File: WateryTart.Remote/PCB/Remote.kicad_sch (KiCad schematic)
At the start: 24 parts, among them J1 Conn_01x04, J2 Conn_01x06, SW1 SW_Push, U1 lolin32_lite_V1.00

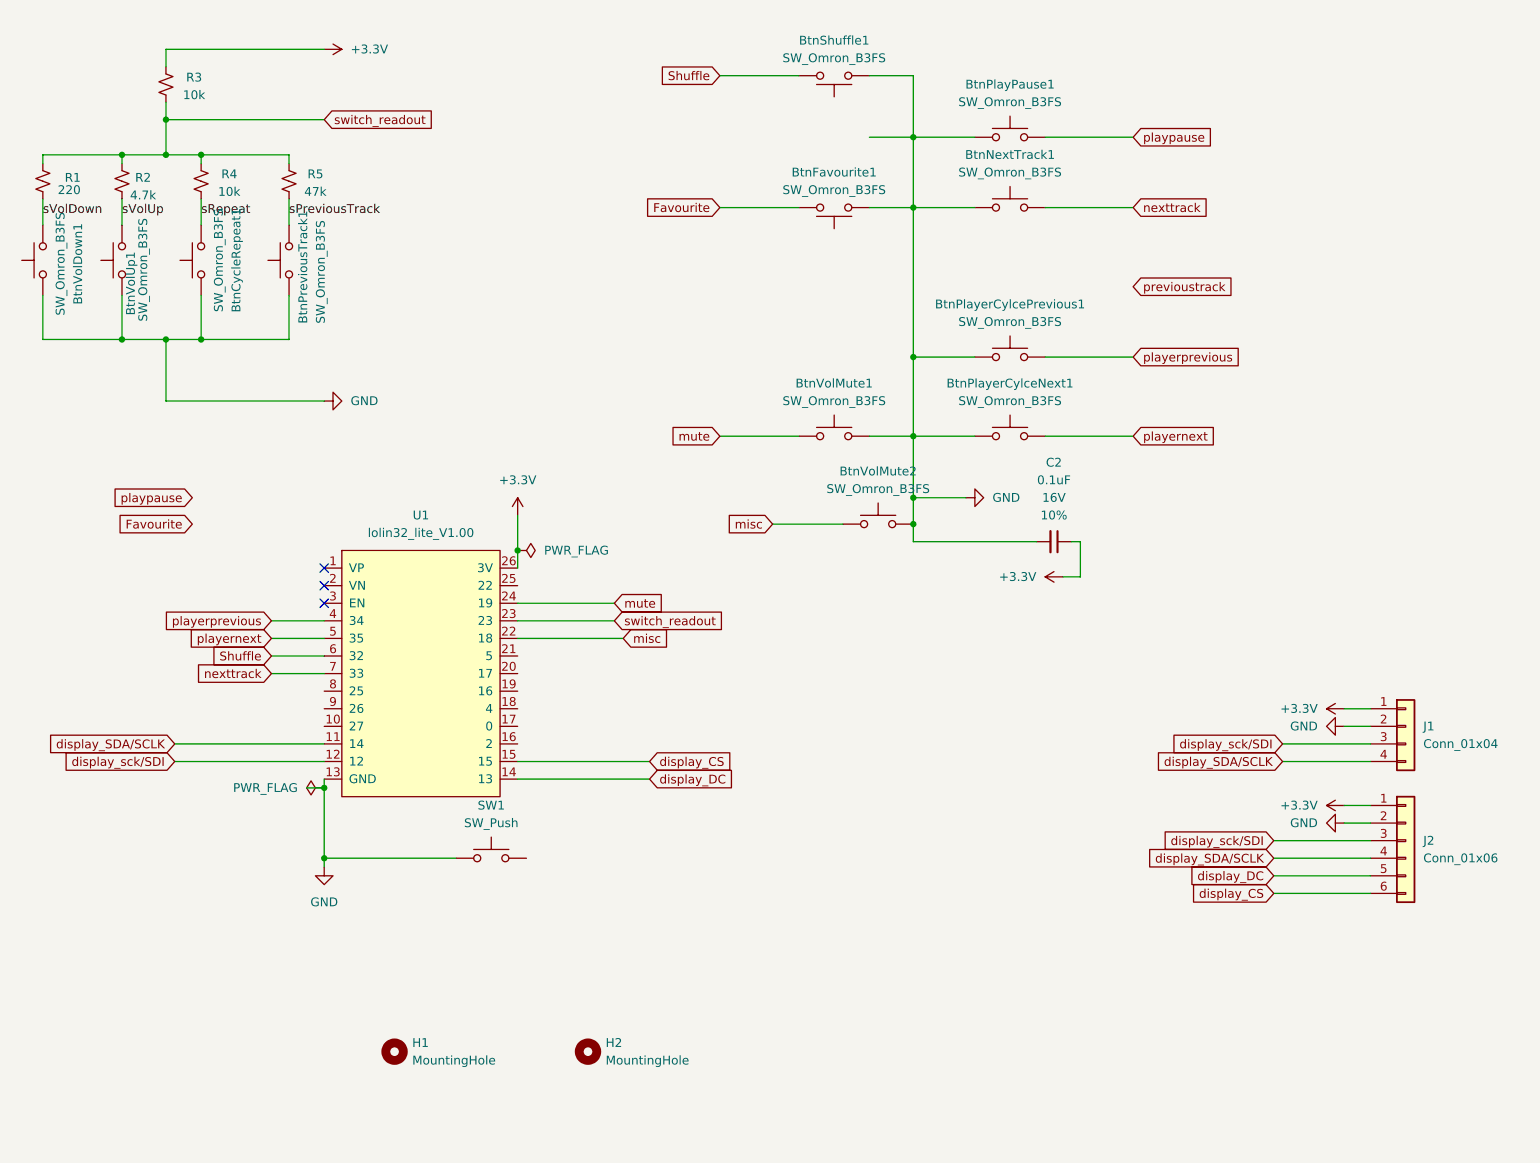
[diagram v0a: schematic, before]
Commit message: Finalised schematic and pcb layout ready for first round of mfg
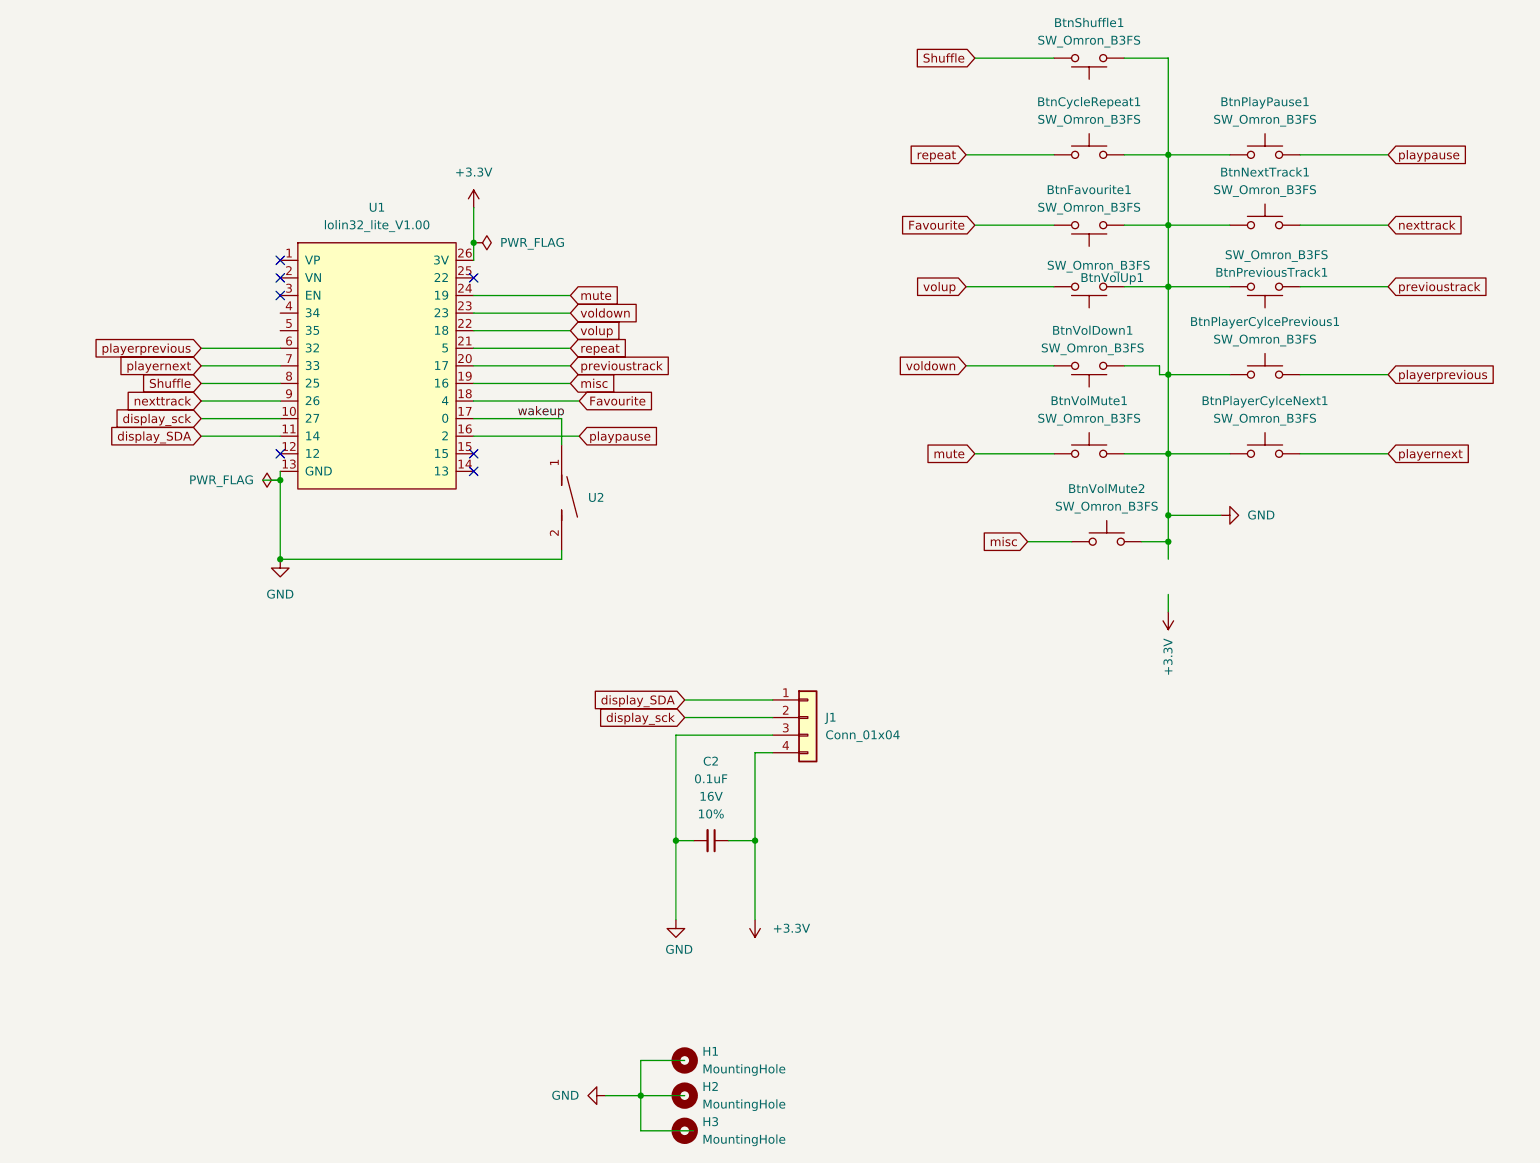
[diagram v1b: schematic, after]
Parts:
- removed J2: Conn_01x06, PCM_SparkFun-Connector:1x06_P2.54mm, symbol PCM_SparkFun-Connector:Conn_01x06_P2.54mm_Socket_Vertical_SMD_Combined
- removed R1: 220, Resistor_THT:R_Axial_DIN0204_L3.6mm_D1.6mm_P5.08mm_Horizontal, symbol PCM_SparkFun-Resistor:3.3k_0402
- removed R2: 4.7k, Resistor_THT:R_Axial_DIN0204_L3.6mm_D1.6mm_P5.08mm_Horizontal, symbol PCM_SparkFun-Resistor:10k_0402
- removed R3, R4: 10k, Resistor_THT:R_Axial_DIN0204_L3.6mm_D1.6mm_P5.08mm_Horizontal, symbol PCM_SparkFun-Resistor:10k_0402
- removed R5: 47k, Resistor_THT:R_Axial_DIN0204_L3.6mm_D1.6mm_P5.08mm_Horizontal, symbol PCM_SparkFun-Resistor:10k_0402
- removed SW1: SW_Push, Resistor_THT:R_Axial_DIN0204_L3.6mm_D1.6mm_P5.08mm_Horizontal, symbol Switch:SW_Push
- added H3: MountingHole, MountingHole:MountingHole_3.2mm_M3_Pad, symbol Mechanical:MountingHole
- added U2: (no value), EasyEDA_Lib:SW-TH_BD3.6-L10.6-LS12.6-D0.4, symbol EasyEDA_Lib:SW-200D 053
- J1: footprint PCM_SparkFun-Connector:1x04_P2.54mm -> Connector_PinSocket_2.54mm:PinSocket_1x04_P2.54mm_Vertical
- U1: footprint PaulsCoolKicadLibrary:WEMOS_LOLIN32_LITE -> Paul:WEMOS_LOLIN32_LITE
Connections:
- net sPreviousTrack is gone; now on net GND: BtnPreviousTrack1.2
- net sRepeat is gone; now on net GND: BtnCycleRepeat1.2
- net switch_readout is gone; now on net voldown: U1.23
- net +3.3V: now also J1.4 (Pin_4); no longer J1.1 (Pin_1)
- net Favourite: now also U1.18 (4)
- net GND: now also J1.3 (Pin_3), U2.2; no longer BtnCycleRepeat1.1, BtnPreviousTrack1.1, J1.2 (Pin_2)
- net Shuffle: now also U1.8 (25); no longer U1.6 (32)
- net misc: now also U1.19 (16); no longer U1.22 (18)
- net nexttrack: now also U1.9 (26); no longer U1.7 (33)
- net playernext: now also U1.7 (33); no longer U1.5 (35)
- net playerprevious: now also U1.6 (32); no longer U1.4 (34)
- net playpause: now also U1.16 (2)
- net previoustrack: now also BtnPreviousTrack1.1, U1.20 (17)
- net voldown: now reaches BtnVolDown1.2
- net display_sck: now reaches U1.10 (27)
- net display_sck: now also J1.2 (Pin_2)
- net wakeup: now reaches U1.17 (0)
- net wakeup: now also U2.1
- net repeat: now reaches U1.21 (5)
- net repeat: now also BtnCycleRepeat1.1
- net display_CS: no longer names the net of U1.15
- net display_DC: no longer names the net of U1.14 (13)
- net display_SDA/SCLK renamed display_SDA
- net display_SDA: now also J1.1 (Pin_1); no longer J1.4 (Pin_4)
- net display_sck/SDI: no longer names the net of U1.12
- net display_sck/SDI: no longer J1.3 (Pin_3)
- net sVolUp renamed volup
- net volup: now also U1.22 (18)
- no-connect marks 3 -> 7
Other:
- moved on the sheet: BtnCycleRepeat1, BtnFavourite1, BtnNextTrack1, BtnPlayPause1, BtnPlayerCylceNext1, BtnPlayerCylcePrevious1, BtnPreviousTrack1, BtnShuffle1, BtnVolDown1, BtnVolMute1, BtnVolMute2, BtnVolUp1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
